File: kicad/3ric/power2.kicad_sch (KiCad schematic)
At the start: 12 parts

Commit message: cleaning up of the schematic
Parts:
- removed U? (x3): 74LS04, symbol 74xx:74LS04
- removed U?: 74LS86, symbol 74xx:74LS86
- added A3, B1, E2, F7, J1_AND1: 74LS08, Package_DIP:DIP-14_W7.62mm_Socket, symbol 74xx:74LS08
- added B3, D1, E4: 74LS32, Package_DIP:DIP-14_W7.62mm_Socket, symbol 74xx:74LS32
- added C2, N7_NOT1: 74LS04, Package_DIP:DIP-14_W7.62mm_Socket, symbol 74xx:74LS04
- added E3, F6: 74LS00, Package_DIP:DIP-14_W7.62mm_Socket, symbol 74xx:74LS00
- added N2_NOT_SIG1: 74LS14, Package_DIP:DIP-14_W7.62mm_Socket, symbol 74xx:74LS14
- C5, E5, W2, W3, W4, W5, W6, W8: renamed from U?; footprint (none) -> Package_DIP:DIP-14_W7.62mm_Socket
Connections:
- net GND: now also A3.7 (GND), B1.7 (GND), B3.7 (GND), C2.7 (GND), D1.7 (GND), E2.7 (GND), E3.7 (GND), E4.7 (GND), F6.7 (GND), F7.7 (GND), J1_AND1.7 (GND), N2_NOT_SIG1.7 (GND), N7_NOT1.7 (GND)
- net VCC: now also A3.14 (VCC), B1.14 (VCC), B3.14 (VCC), C2.14 (VCC), D1.14 (VCC), E2.14 (VCC), E3.14 (VCC), E4.14 (VCC), F6.14 (VCC), F7.14 (VCC), J1_AND1.14 (VCC), N2_NOT_SIG1.14 (VCC), N7_NOT1.14 (VCC)
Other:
- moved on the sheet: C5E, E5E, W2G, W3E, W4E, W5E, W6E, W8E

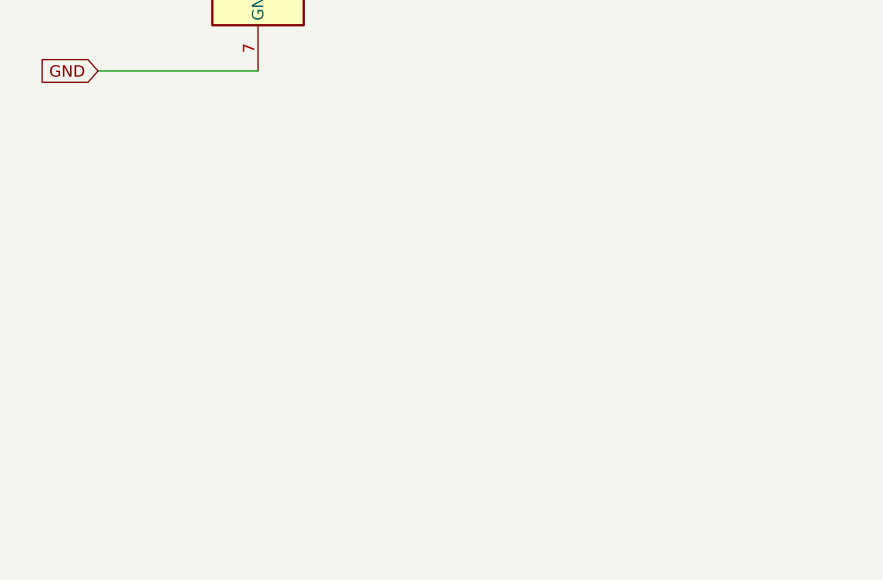
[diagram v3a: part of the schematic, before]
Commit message: updated schematics and PCB PNG of the breadboard layout
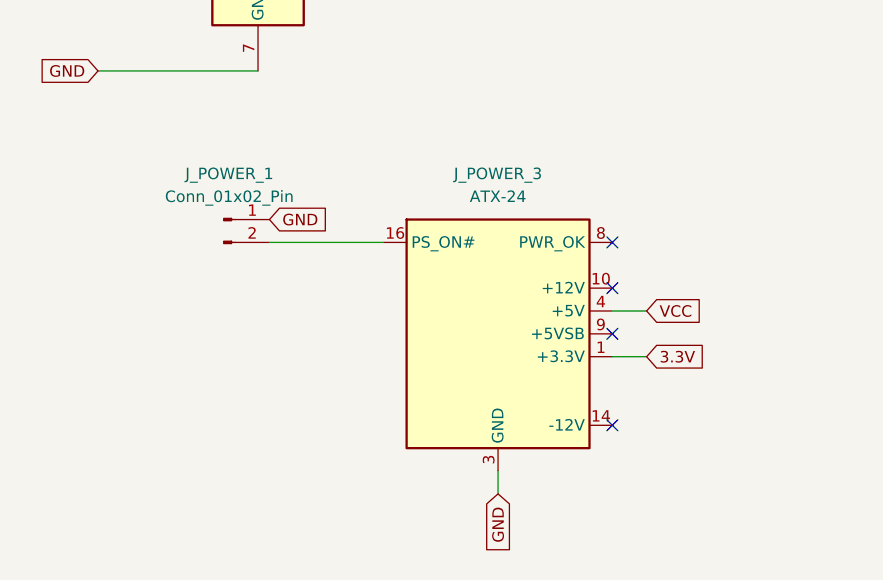
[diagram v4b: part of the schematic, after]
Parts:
- added J_POWER_1: Conn_01x02_Pin, Connector_PinHeader_2.54mm:PinHeader_2x01_P2.54mm_Vertical, symbol Connector:Conn_01x02_Pin
- added J_POWER_3: ATX-24, atxplug:1-1775099-3, symbol Connector:ATX-24
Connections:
- net GND: now also J_POWER_1.1 (Pin_1), J_POWER_3.15 (GND), J_POWER_3.17 (GND), J_POWER_3.18 (GND), J_POWER_3.19 (GND), J_POWER_3.24 (GND), J_POWER_3.3 (GND), J_POWER_3.5 (GND), J_POWER_3.7 (GND)
- net VCC: now also J_POWER_3.21 (+5V), J_POWER_3.22 (+5V), J_POWER_3.23 (+5V), J_POWER_3.4 (+5V), J_POWER_3.6 (+5V)
- new net: J_POWER_3.10 (+12V), J_POWER_3.11 (+12V)
- new net: J_POWER_1.2 (Pin_2), J_POWER_3.16 (PS_ON#)
- new net 3.3V: J_POWER_3.1 (+3.3V), J_POWER_3.12 (+3.3V), J_POWER_3.13 (+3.3V), J_POWER_3.2 (+3.3V)
- no-connect marks 0 -> 4

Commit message: pcb layout continued
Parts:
- added C58: 0.1µ, Capacitor_SMD:C_1206_3216Metric_Pad1.33x1.80mm_HandSolder, symbol Device:C
- added J_PWR_LED_1: Conn_01x02_Pin, Connector_PinHeader_2.54mm:PinHeader_2x01_P2.54mm_Vertical, symbol Connector:Conn_01x02_Pin
- added R23: R, Resistor_SMD:R_0603_1608Metric_Pad0.98x0.95mm_HandSolder, symbol Device:R
- added R_POWER1: 1K, Resistor_SMD:R_0603_1608Metric_Pad0.98x0.95mm_HandSolder, symbol Device:R
- added U1: 74HC74, Package_DIP:DIP-14_W7.62mm_Socket, symbol 74xx:74HC74
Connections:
- net GND: now also C58.1, R23.1, R_POWER1.1, U1.7 (GND); no longer J_POWER_1.1 (Pin_1)
- net VCC: now also J_PWR_LED_1.1 (Pin_1)
- net at J_POWER_3.16 (PS_ON#): now also U1.2 (D), U1.6 (~{Q}); no longer J_POWER_1.2 (Pin_2)
- net at J_POWER_3.9 (+5VSB): now also J_POWER_1.1 (Pin_1), U1.1 (~{R}), U1.14 (VCC), U1.4 (~{S})
- new net: C58.2, J_POWER_1.2 (Pin_2), R_POWER1.2, U1.3 (C)
- new net: J_PWR_LED_1.2 (Pin_2), R23.2
- no-connect marks 4 -> 10
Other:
- moved on the sheet: J1_AND1E, J_POWER_3

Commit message: v2 pcb
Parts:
- removed F7: 74LS08, Package_DIP:DIP-14_W7.62mm_Socket, symbol 74xx:74LS08
- R23: value R -> R220
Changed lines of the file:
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@@
 	)
 	(junction
-		(at 250.19 48.26)
-		(diameter 0)
-		(color 0 0 0 0)
-	)
-	(junction
 		(at 205.74 48.26)
 		(diameter 0)
@@
 	)
 	(junction
-		(at 250.19 22.86)
-		(diameter 0)
-		(color 0 0 0 0)
-	)
-	(junction
 		(at 139.7 129.54)
 		(diameter 0)
@@
 	(wire
 		(pts
-			(xy 227.33 22.86) (xy 250.19 22.86)
+			(xy 227.33 22.86) (xy 269.24 22.86)
 		)
 		(stroke
@@
 	(wire
 		(pts
-			(xy 250.19 22.86) (xy 269.24 22.86)
-		)
-		(stroke
-			(width 0)
-			(type default)
-		)
-	)
-	(wire
-		(pts
 			(xy 153.67 106.68) (xy 182.88 106.68)
 		)
@@
 	(wire
 		(pts
-			(xy 227.33 48.26) (xy 250.19 48.26)
+			(xy 227.33 48.26) (xy 269.24 48.26)
 		)
 		(stroke
@@
 	(wire
 		(pts
-			(xy 250.19 48.26) (xy 269.24 48.26)
-		)
-		(stroke
-			(width 0)
-			(type default)
-		)
-	)
-	(wire
-		(pts
 			(xy 168.91 111.76) (xy 139.7 111.76)
 		)
@@
 	)
 	(symbol
-		(lib_id "74xx:74LS08")
-		(at 250.19 35.56 0)
-		(unit 5)
-		(exclude_from_sim no)
-		(in_bom yes)
-		(on_board yes)
-		(dnp no)
-		(fields_autoplaced yes)
-		(property "Reference" "F7"
-			(at 256.032 34.7253 0)
-			(effects
-				(font
-					(size 1.27 1.27)
-				)
-				(justify left)
-			)
-		)
-		(property "Value" "74LS08"
-			(at 256.032 37.2622 0)
-			(effects
-				(font
-					(size 1.27 1.27)
-				)
-				(justify left)
-			)
-		)
-		(property "Footprint" "Package_DIP:DIP-14_W7.62mm_Socket"
-			(at 250.19 35.56 0)
-			(effects
-				(font
-					(size 1.27 1.27)
-				)
-				(hide yes)
-			)
-		)
-		(property "Datasheet" "http://www.ti.com/lit/gpn/sn74LS08"
-			(at 250.19 35.56 0)
-			(effects
-				(font
-					(size 1.27 1.27)
-				)
-				(hide yes)
-			)
-		)
-		(property "Description" ""
-			(at 250.19 35.56 0)
-			(effects
-				(font
-					(size 1.27 1.27)
-				)
-				(hide yes)
-			)
-		)
-		(pin "1"
-		)
-		(pin "2"
-		)
-		(pin "3"
-		)
-		(pin "4"
-		)
-		(pin "5"
-		)
-		(pin "6"
-		)
-		(pin "10"
-		)
-		(pin "8"
-		)
-		(pin "9"
-		)
-		(pin "11"
-		)
-		(pin "12"
-		)
-		(pin "13"
-		)
-		(pin "14"
-		)
-		(pin "7"
-		)
-		(instances
-			(project "3ric"
-				(path "/e63e39d7-6ac0-4ffd-8aa3-1841a4541b55/3d1988b8-66f2-463c-870d-4e35da6e7dd8"
-					(reference "F7")
-					(unit 5)
-				)
-			)
-		)
-	)
-	(symbol
 		(lib_id "74xx:74LS04")
 		(at 43.18 114.3 0)
@@
 			)
 		)
-		(property "Value" "R"
+		(property "Value" "R220"
 			(at 218.44 109.22 90)
 			(effects
